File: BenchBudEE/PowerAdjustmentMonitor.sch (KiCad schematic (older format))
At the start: 18 parts, among them U10 LM7805, U11 LM317, U7 LM324, U8 LM317, U9 LM7805

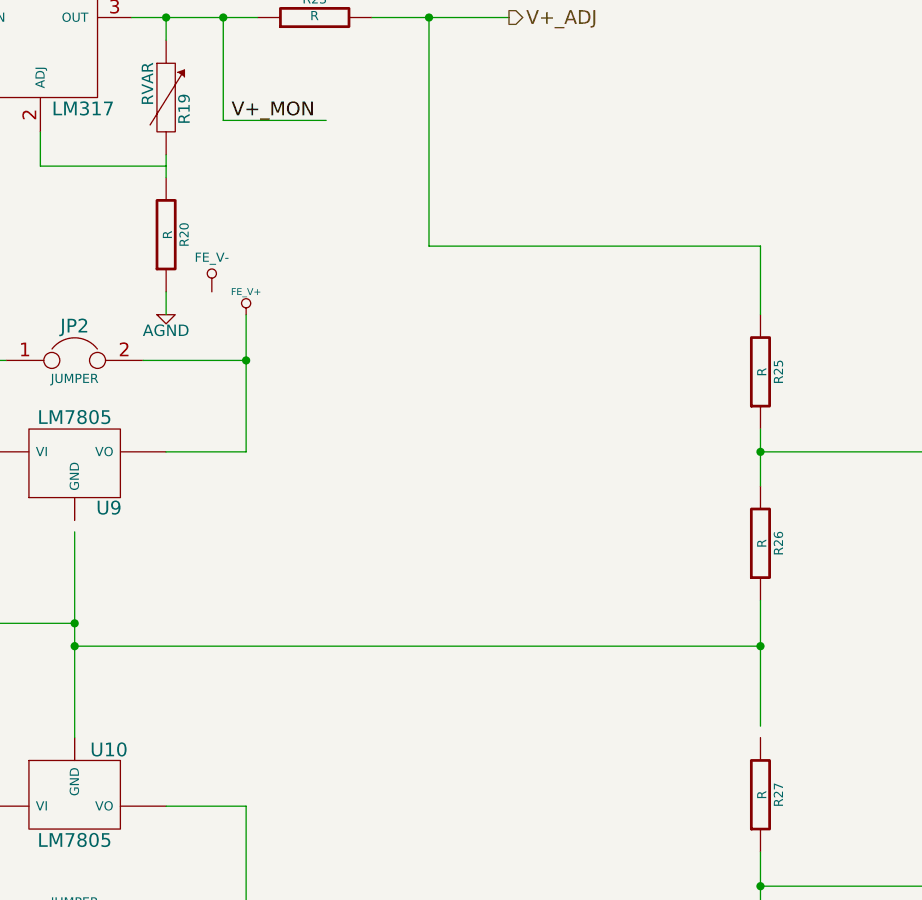
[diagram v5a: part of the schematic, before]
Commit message: Arduino module associated + roughly placed.
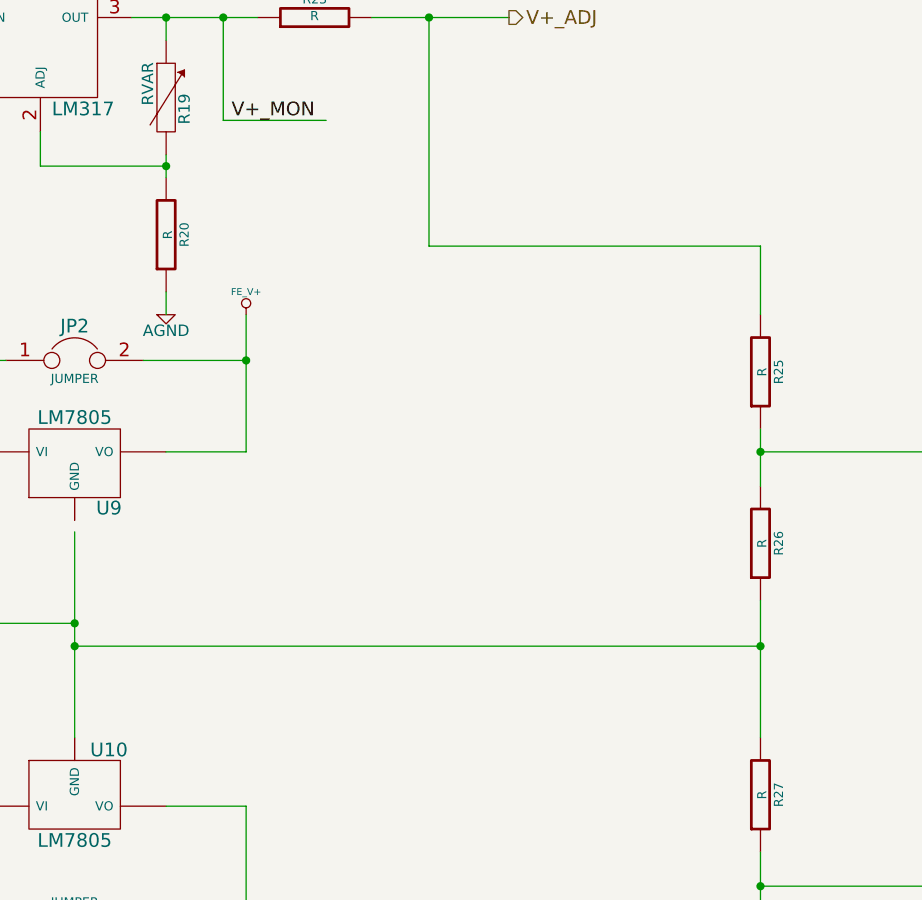
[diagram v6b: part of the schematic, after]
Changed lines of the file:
@@
 Sheet 8 9
 Title ""
-Date "20 feb 2014"
+Date "23 feb 2014"
 Rev ""
 Comp ""
@@
 $EndDescr
 $Comp
-L +3.3V #PWR038
+L +3.3V #PWR045
 U 1 1 52F30EBD
 P 8050 2750
-F 0 "#PWR038" H 8050 2710 30  0001 C CNN
+F 0 "#PWR045" H 8050 2710 30  0001 C CNN
 F 1 "+3.3V" H 8050 2860 30  0000 C CNN
 F 2 "" H 8050 2750 60  0000 C CNN
@@
 $EndComp
 $Comp
-L +5V #PWR039
+L +5V #PWR046
 U 1 1 52F30EC3
 P 7850 2750
-F 0 "#PWR039" H 7850 2840 20  0001 C CNN
+F 0 "#PWR046" H 7850 2840 20  0001 C CNN
 F 1 "+5V" H 7850 2840 30  0000 C CNN
 F 2 "" H 7850 2750 60  0000 C CNN
@@
 $EndComp
 $Comp
-L +12V #PWR040
+L +12V #PWR047
 U 1 1 52F31364
 P 1850 2850
-F 0 "#PWR040" H 1850 2800 20  0001 C CNN
+F 0 "#PWR047" H 1850 2800 20  0001 C CNN
 F 1 "+12V" H 1850 2950 30  0000 C CNN
 F 2 "" H 1850 2850 60  0000 C CNN
@@
 $EndComp
 $Comp
-L -12V #PWR041
+L -12V #PWR048
 U 1 1 52F31373
 P 1850 4800
-F 0 "#PWR041" H 1850 4930 20  0001 C CNN
+F 0 "#PWR048" H 1850 4930 20  0001 C CNN
 F 1 "-12V" H 1850 4900 30  0000 C CNN
 F 2 "" H 1850 4800 60  0000 C CNN
@@
 $EndComp
 $Comp
-L GND #PWR042
+L GND #PWR049
 U 1 1 52F315E7
 P 700 4100
-F 0 "#PWR042" H 700 4100 30  0001 C CNN
+F 0 "#PWR049" H 700 4100 30  0001 C CNN
 F 1 "GND" H 700 4030 30  0001 C CNN
 F 2 "" H 700 4100 60  0000 C CNN
@@
 $EndComp
 $Comp
-L AGND #PWR043
+L AGND #PWR050
 U 1 1 52F315F6
 P 1400 4100
-F 0 "#PWR043" H 1400 4100 40  0001 C CNN
+F 0 "#PWR050" H 1400 4100 40  0001 C CNN
 F 1 "AGND" H 1400 4030 50  0000 C CNN
 F 2 "" H 1400 4100 60  0000 C CNN
@@
 $EndComp
 $Comp
-L FE_V+ #PWR044
+L FE_V+ #PWR051
 U 1 1 52F316C5
 P 3350 2350
-F 0 "#PWR044" H 3350 2450 30  0001 C CNN
+F 0 "#PWR051" H 3350 2450 30  0001 C CNN
 F 1 "FE_V+" H 3350 2450 30  0000 C CNN
 F 2 "" H 3350 2350 60  0000 C CNN
@@
 $EndComp
 $Comp
-L FE_V- #PWR47
+L FE_V- #PWR54
 U 1 1 52F316D4
 P 3350 5200
-F 0 "#PWR47" H 3350 5400 40  0001 C CNN
+F 0 "#PWR54" H 3350 5400 40  0001 C CNN
 F 1 "FE_V-" H 3350 5350 40  0000 C CNN
 F 2 "" H 3350 5200 60  0000 C CNN
@@
 $EndComp
 $Comp
-L AGND #PWR045
+L AGND #PWR052
 U 1 1 52F31737
 P 2050 4000
-F 0 "#PWR045" H 2050 4000 40  0001 C CNN
+F 0 "#PWR052" H 2050 4000 40  0001 C CNN
 F 1 "AGND" H 2050 3930 50  0000 C CNN
 F 2 "" H 2050 4000 60  0000 C CNN
@@
 $EndComp
 $Comp
-L FE_V- #PWR45
-U 1 1 52F318F5
-P 3200 2250
-F 0 "#PWR45" H 3200 2450 40  0001 C CNN
-F 1 "FE_V-" H 3200 2400 40  0000 C CNN
-F 2 "" H 3200 2250 60  0000 C CNN
-F 3 "" H 3200 2250 60  0000 C CNN
-	1    3200 2250
-	1    0    0    -1
-$EndComp
-$Comp
 L R R20
 U 1 1 52F31901
@@
 $EndComp
 $Comp
-L AGND #PWR046
+L AGND #PWR053
 U 1 1 52F3195F
 P 2700 5550
-F 0 "#PWR046" H 2700 5550 40  0001 C CNN
+F 0 "#PWR053" H 2700 5550 40  0001 C CNN
 F 1 "AGND" H 2700 5480 50  0000 C CNN
 F 2 "" H 2700 5550 60  0000 C CNN
@@
 $EndComp
 $Comp
-L AGND #PWR047
+L AGND #PWR054
 U 1 1 52F319EB
 P 3000 2350
-F 0 "#PWR047" H 3000 2350 40  0001 C CNN
+F 0 "#PWR054" H 3000 2350 40  0001 C CNN
 F 1 "AGND" H 3000 2280 50  0000 C CNN
 F 2 "" H 3000 2350 60  0000 C CNN
@@
 $EndComp
 $Comp
-L +12V #PWR048
+L +12V #PWR055
 U 1 1 52F320CB
 P 9250 5450
-F 0 "#PWR048" H 9250 5400 20  0001 C CNN
+F 0 "#PWR055" H 9250 5400 20  0001 C CNN
 F 1 "+12V" H 9250 5550 30  0000 C CNN
 F 2 "" H 9250 5450 60  0000 C CNN
@@
 $EndComp
 $Comp
-L -12V #PWR049
+L -12V #PWR056
 U 1 1 52F320D1
 P 9250 6450
-F 0 "#PWR049" H 9250 6580 20  0001 C CNN
+F 0 "#PWR056" H 9250 6580 20  0001 C CNN
 F 1 "-12V" H 9250 6550 30  0000 C CNN
 F 2 "" H 9250 6450 60  0000 C CNN
@@
 $EndComp
 $Comp
-L +12V #PWR050
+L +12V #PWR057
 U 1 1 52F32180
 P 9250 3850
-F 0 "#PWR050" H 9250 3800 20  0001 C CNN
+F 0 "#PWR057" H 9250 3800 20  0001 C CNN
 F 1 "+12V" H 9250 3950 30  0000 C CNN
 F 2 "" H 9250 3850 60  0000 C CNN
@@
 $EndComp
 $Comp
-L -12V #PWR051
+L -12V #PWR058
 U 1 1 52F32186
 P 9250 4850
-F 0 "#PWR051" H 9250 4980 20  0001 C CNN
+F 0 "#PWR058" H 9250 4980 20  0001 C CNN
 F 1 "-12V" H 9250 4950 30  0000 C CNN
 F 2 "" H 9250 4850 60  0000 C CNN
@@
 Wire Wire Line
 	2450 1550 2450 1700
-Wire Wire Line
-	2450 1700 3000 1700
 Connection ~ 3000 1050
 Connection ~ 2050 2550
@@
 	5600 2850 5600 3100
 Wire Wire Line
-	5600 3600 5600 4150
+	5600 3600 5600 4200
 Wire Wire Line
 	5600 3800 2600 3800
@@
 Wire Wire Line
 	3000 1650 3000 1750
+Wire Wire Line
+	2450 1700 3000 1700
+Connection ~ 3000 1700
 $EndSCHEMATC

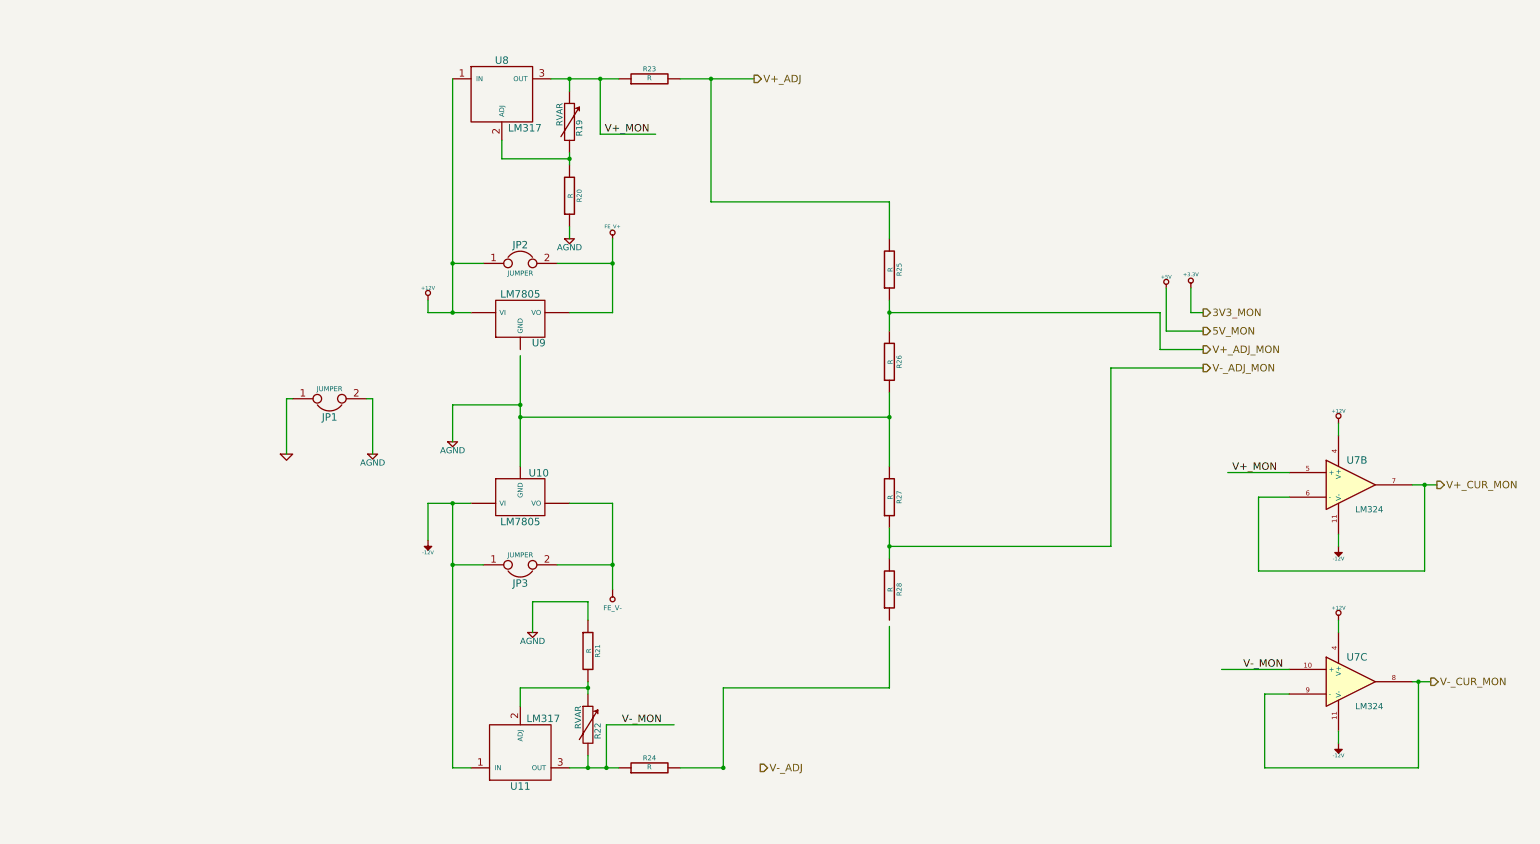
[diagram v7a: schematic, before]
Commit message: All modules (inc. LED Driver) associated + roughly placed.
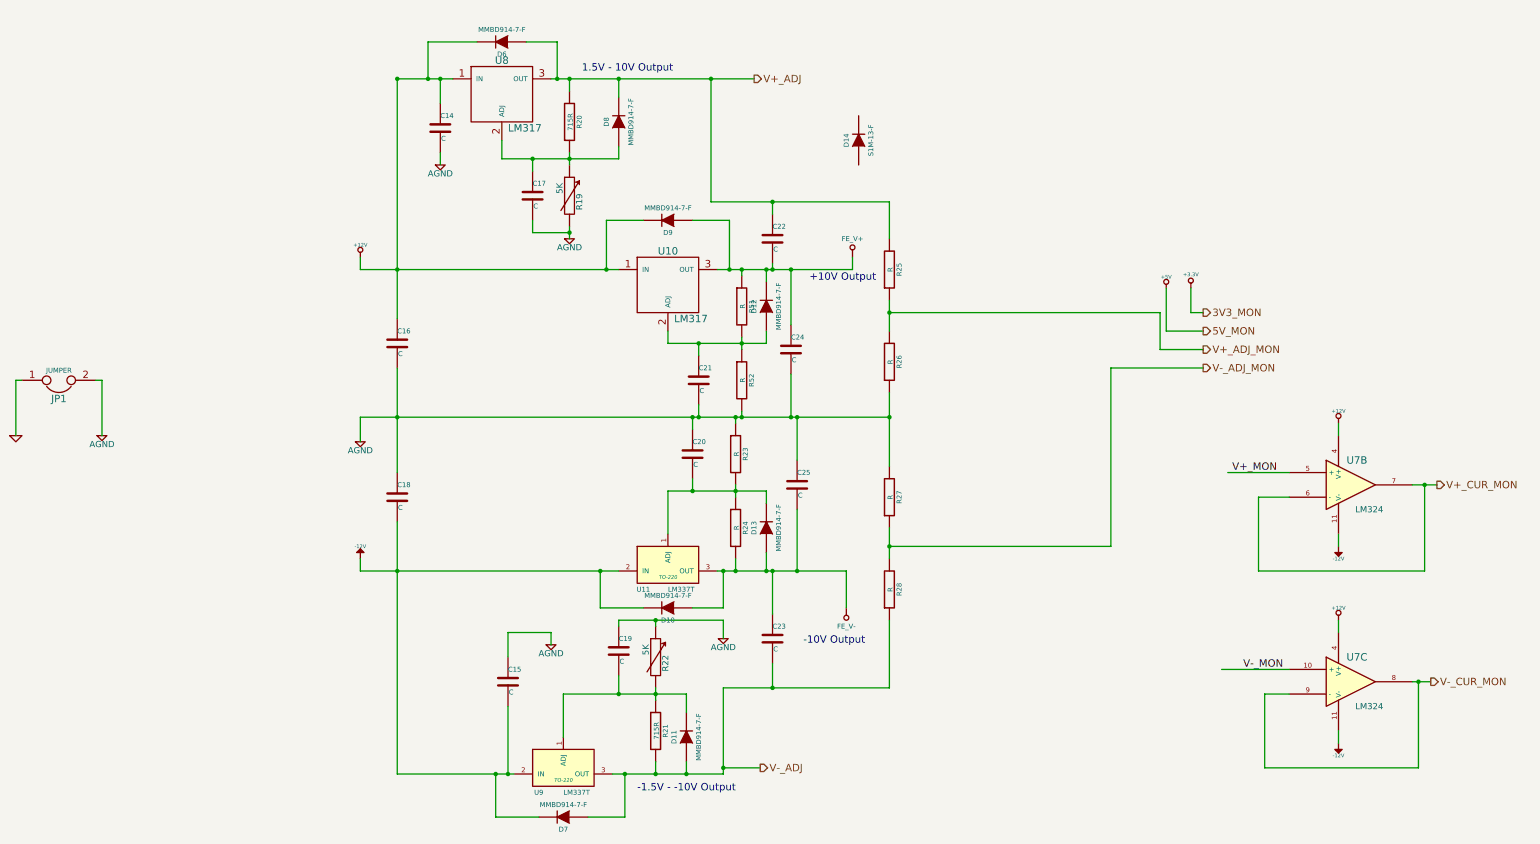
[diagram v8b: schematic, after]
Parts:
- removed JP2, JP3: JUMPER, ~, symbol JUMPER
- removed U10, U9: LM7805, ~, symbol LM7805
- removed U11: LM317, ~, symbol LM317
- added C14, C15, C16, C17, C18, C19, C20, C21, C22, C23, C24, C25: C, ~, symbol C
- added D10, D11, D12, D13, D6, D7, D8, D9: MMBD914-7-F, ~, symbol DIODE
- added D14: S1M-13-F, ~, symbol DIODE
- added R51, R52: R, ~, symbol R
- added U10: LM317, ~, symbol LM317
- added U11, U9: LM337T, TO-220, symbol LM337T
- R19, R22: value RVAR -> 5K; Distributor (none) -> DigiKey; Distributor Part Link (none) -> http://www.digikey.com/product-detail/en/EVU-E3KFK4B53/P3W1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; Distributor Part Number (none) -> P3W1502-ND; MFG Name (none) -> Panasonic Electronic Components; MFG Part Number (none) -> EVU-E3KFK4B53
- R20, R21: value R -> 715R
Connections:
- wire segments 78 -> 126
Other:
- note added: "+10V Output"
- note added: "-1.5V - -10V Output"
- note added: "-10V Output"
- note added: "1.5V - 10V Output"
- moved on the sheet: JP1, R19, R20
